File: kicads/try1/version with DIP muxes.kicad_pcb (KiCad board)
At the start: 2 copper layers, 166.5 x 100 mm, 48 parts, among them P1 CONN_01X08, P10 CONN_01X08, P11 CONN_01X08, P12 CONN_01X08, P13 CONN_01X08, P14 CONN_01X08, P15 CONN_01X08, P16 CONN_01X08, P17 CONN_01X08, P18 CONN_01X08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

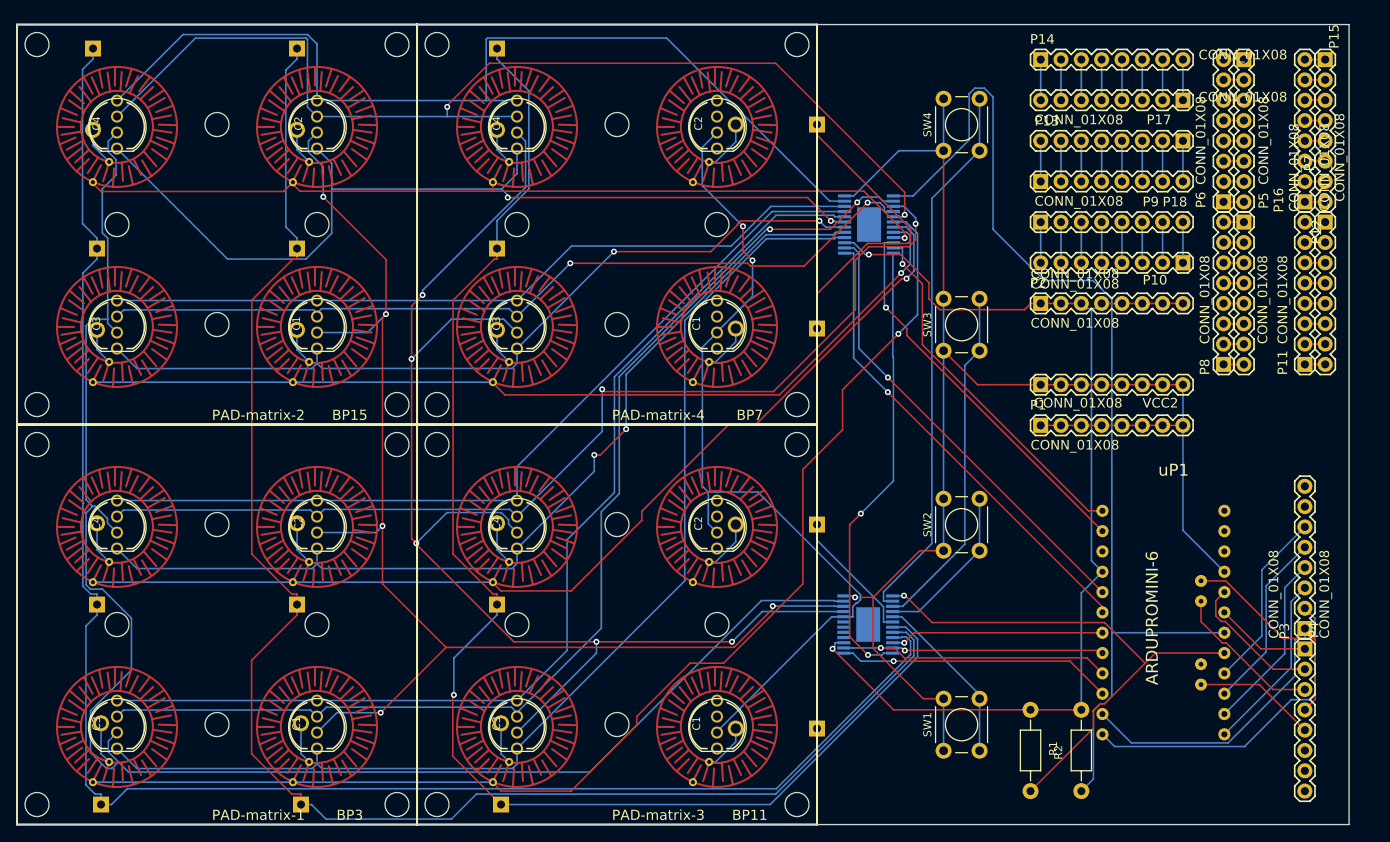
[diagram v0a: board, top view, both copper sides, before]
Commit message: successfully adapted the software for screen+button pad matrix using 16x muxes and arduino
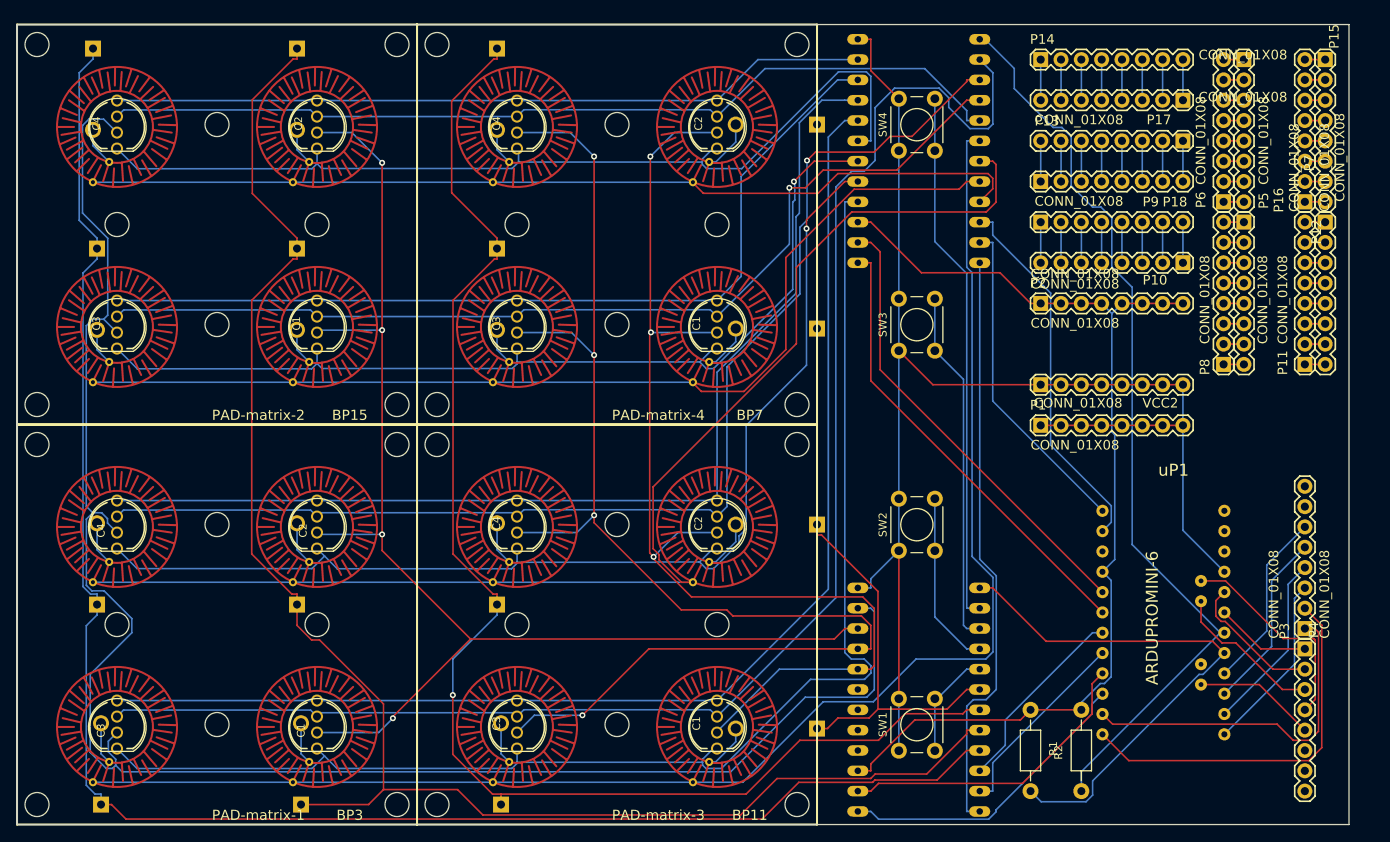
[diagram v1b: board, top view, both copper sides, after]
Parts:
- U2, U3: footprint SparkFun-DigitalIC:TSSOP-24 -> SparkFun-DigitalIC:DIL24-6
- moved U3 11.3 mm to (172.7, 135.9)
- moved U2 11.1 mm to (172.7, 67.3)
- moved SW1 5.59 mm to (170.2, 142.3)
- moved SW2 5.59 mm to (170.2, 117.3)
- moved SW3 5.59 mm to (170.2, 92.3)
- moved SW4 5.59 mm to (170.2, 67.3)
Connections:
- PAD-matrix-3 pad BLU1: Net-(PAD-matrix-3-PadBLU1) -> /MUXAB7
- PAD-matrix-3 pad BLU2: Net-(PAD-matrix-3-PadBLU2) -> /MUXAB6
- PAD-matrix-3 pad GRN1: Net-(PAD-matrix-3-PadGRN1) -> /MUXAG11
- PAD-matrix-3 pad GRN2: Net-(PAD-matrix-3-PadGRN2) -> /MUXAG10
- PAD-matrix-3 pad RED1: Net-(PAD-matrix-3-PadRED1) -> /MUXAR15
- PAD-matrix-3 pad RED2: Net-(PAD-matrix-3-PadRED2) -> /MUXAR14
- PAD-matrix-3 pad SIG1: Net-(PAD-matrix-3-PadSIG1) -> /MUXAS3
- PAD-matrix-3 pad SIG3: Net-(PAD-matrix-3-PadSIG3) -> /MUXAS2
- PAD-matrix-4 pad BLU1: Net-(PAD-matrix-4-PadBLU1) -> /MUXAB5
- PAD-matrix-4 pad BLU2: Net-(PAD-matrix-4-PadBLU2) -> /MUXAB4
- PAD-matrix-4 pad GRN1: Net-(PAD-matrix-4-PadGRN1) -> /MUXAG9
- PAD-matrix-4 pad GRN2: Net-(PAD-matrix-4-PadGRN2) -> /MUXAG8
- PAD-matrix-4 pad RED1: Net-(PAD-matrix-4-PadRED1) -> /MUXAR13
- PAD-matrix-4 pad RED2: Net-(PAD-matrix-4-PadRED2) -> /MUXAR12
- PAD-matrix-4 pad SIG1: Net-(PAD-matrix-4-PadSIG1) -> /MUXAS1
- PAD-matrix-4 pad SIG3: Net-(PAD-matrix-4-PadSIG3) -> /MUXAS0
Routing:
- net /MUXAB7: track 143.0 -> 189.5 mm, vias 2 -> 0
- net /MUXAS3: track 154.0 -> 186.1 mm, vias 1 -> 0
- net /MUXAS2: track 127.8 -> 159.9 mm, vias 1 -> 0
- net /MUXBG11: track 107.3 -> 138.1 mm, vias 2 -> 3
- net /MUXAR15: track 142.1 -> 171.0 mm
- net /MUXAG8: track 121.9 -> 94.7 mm
- net /MUXAG10: track 108.4 -> 135.0 mm
- net /MUXAB6: track 128.7 -> 151.8 mm, vias 2 -> 1
- net /MUXAG11: track 132.7 -> 155.7 mm
- net /MUXAR14: track 118.1 -> 140.4 mm, vias 2 -> 1
- net /MUXAB4: track 134.8 -> 115.1 mm, vias 2 -> 0
- net /MUXAB5: track 105.6 -> 124.6 mm, vias 2 -> 1
- net /A1: track 134.3 -> 115.8 mm
- net GND: track 56.7 -> 73.5 mm, vias 2 -> 0
- net /MUXAR13: track 103.5 -> 120.0 mm, vias 2 -> 1
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
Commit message: adapt portb connection to fit an LCD breakout
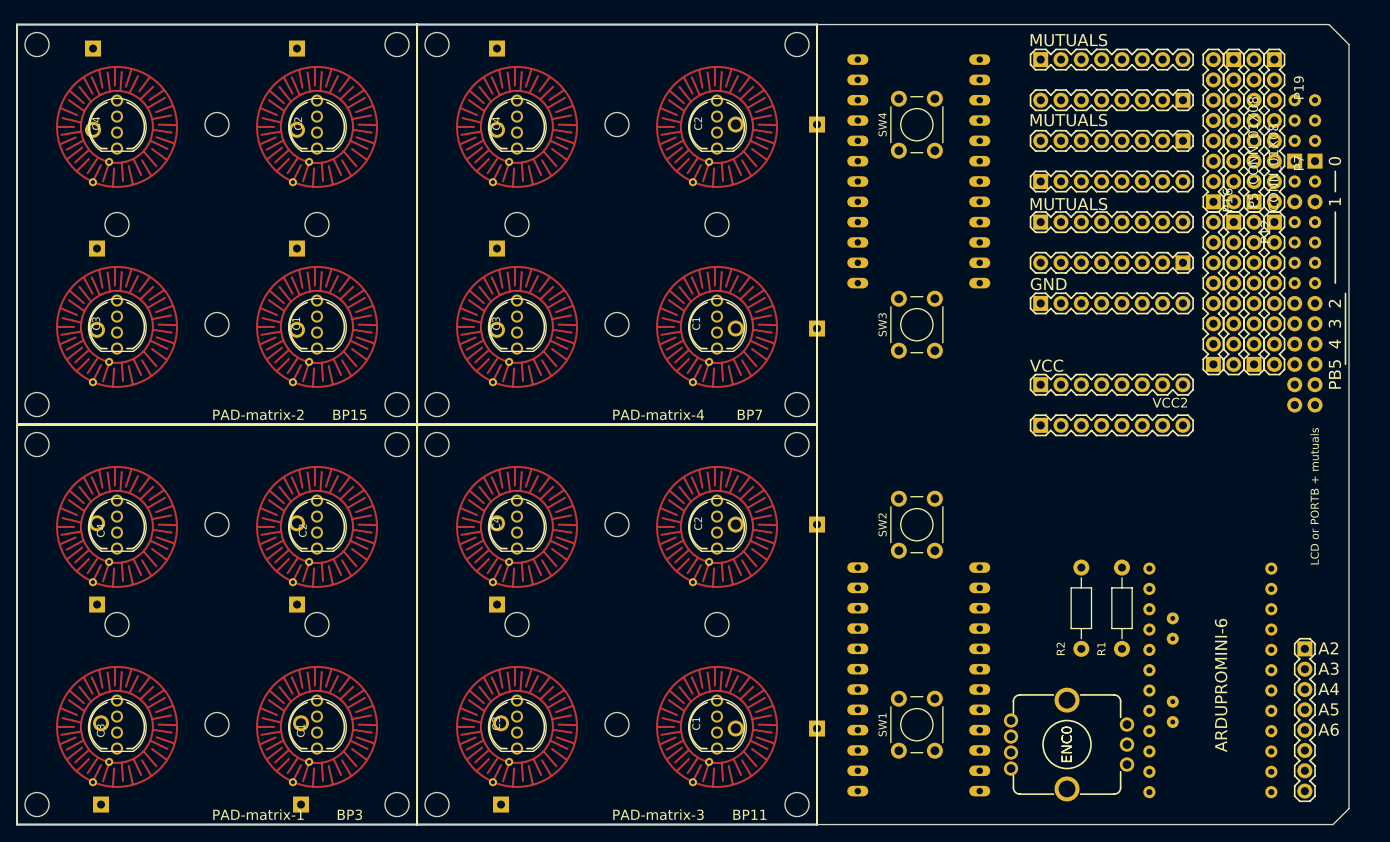
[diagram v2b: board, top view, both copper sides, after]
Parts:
- added ENC0: ENC0, SparkFun-Electromechanical:ENCODER_LED_2, F.Cu at (191.2, 141.5)
- added P19: CONN_01X16, lcd32-breakout-connector:1X08, F.Cu at (219.7, 61.0)
- P3: value CONN_01X08 -> CONN_01X16
- moved P3 66.1 mm to (222.2, 61.0), turned to 270 degrees
- moved uP1 54.6 mm to (219.3, 153.8), turned to 180 degrees
- moved R2 18.9 mm to (193.0, 119.4)
- moved R1 18.5 mm to (198.1, 129.5)
- moved P12 6.35 mm to (217.2, 76.2)
- moved P15 6.35 mm to (217.2, 55.9)
- moved P11 6.35 mm to (214.6, 94.0)
- moved P16 6.35 mm to (214.6, 73.7)
- moved U2 2.54 mm to (172.7, 69.8)
- moved U3 2.54 mm to (172.7, 133.3)
- moved P5 1.27 mm to (212.1, 55.9)
- moved P7 1.27 mm to (212.1, 76.2)
- moved P6 1.27 mm to (209.6, 73.7)
- moved P8 1.27 mm to (209.6, 94.0)
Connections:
- P13 pad 1: Net-(P13-Pad1) -> /MUX12
- P13 pad 2: Net-(P13-Pad2) -> /MUX13
- P13 pad 3: Net-(P13-Pad3) -> /MUX14
- P13 pad 4: Net-(P13-Pad4) -> /MUX15
- P14 pad 5: Net-(P13-Pad4) -> /MUX15
- P14 pad 6: Net-(P13-Pad3) -> /MUX14
- P14 pad 7: Net-(P13-Pad2) -> /MUX13
- P14 pad 8: Net-(P13-Pad1) -> /MUX12
- P2 pad 1: GNDREF -> GND
- P2 pad 2: GNDREF -> GND
- P2 pad 3: GNDREF -> GND
- P2 pad 4: GNDREF -> GND
- P2 pad 5: GNDREF -> GND
- P2 pad 6: GNDREF -> GND
- P2 pad 7: GNDREF -> GND
- P2 pad 8: GNDREF -> GND
- R1 pad 2: GNDREF -> GND
- R2 pad 1: GNDREF -> GND
- U2 pad 15: GNDREF -> GND
- U3 pad 15: GNDREF -> GND
- uP1 pad 10: GNDREF -> GND
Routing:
- net /MUXBG8: track 220.2 -> 0.00 mm
- net /MUXBS0: track 214.0 -> 0.00 mm
- net /MUXBS1: track 199.6 -> 0.00 mm
- net /MUXAB7: track 189.5 -> 0.00 mm
- net /MUXAS3: track 186.1 -> 0.00 mm
- net /VCC: track 180.3 -> 0.00 mm
- net /MUXBS2: track 174.1 -> 0.00 mm, vias 1 -> 0
- net /MUXAR15: track 171.0 -> 0.00 mm
- net /MUXBG10: track 169.4 -> 0.00 mm, vias 4 -> 0
- net /MUXBG9: track 163.4 -> 0.00 mm, vias 4 -> 0
- net /MUXAS2: track 159.9 -> 0.00 mm
- net /MUXAG11: track 155.7 -> 0.00 mm
- net /MUXAB6: track 151.8 -> 0.00 mm, vias 1 -> 0
- net /MUXAR14: track 140.4 -> 0.00 mm, vias 1 -> 0
- net /MUXBG11: track 138.1 -> 0.00 mm, vias 3 -> 0
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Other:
- outline, holes or cut-outs redrawn
- board text added: "0"
- board text added: "1"
- board text added: "2"
- board text added: "3"
- board text added: "4"
- board text added: "A2"
- board text added: "A3"
- board text added: "A4"
- board text added: "A5"
- board text added: "A6"
- board text added: "GND"
- board text added: "MUTUALS"
- board text added: "PB5"
- board text added: "VCC"

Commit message: routed last schematic change in the dip version
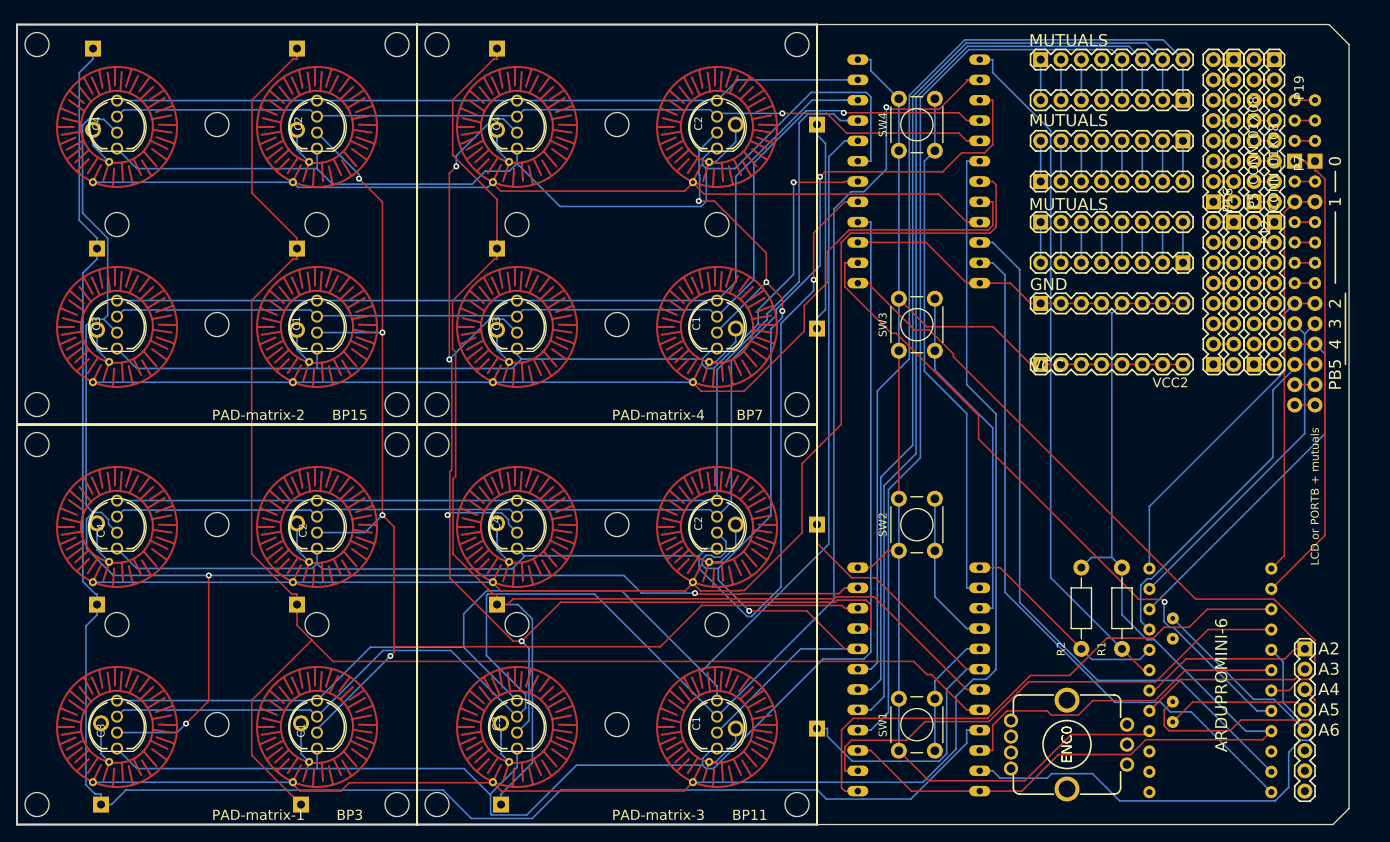
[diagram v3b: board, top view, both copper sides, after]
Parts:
- removed P1: CONN_01X08, SparkFun-Connectors:1X08
- moved CONN_01X08 2.54 mm to (188.0, 94.0)
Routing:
- net /MUXBS0: track 0.00 -> 218.0 mm
- net /MUXAB7: track 0.00 -> 209.6 mm, vias 0 -> 1
- net /MUXBS1: track 0.00 -> 198.3 mm
- net /MUXBG8: track 0.00 -> 196.7 mm, vias 0 -> 3
- net /MUXAS3: track 0.00 -> 191.2 mm
- net /MUXBS2: track 0.00 -> 177.5 mm
- net /MUXAR15: track 0.00 -> 176.0 mm
- net /MUXAG11: track 0.00 -> 174.6 mm
- net /VCC: track 0.00 -> 169.8 mm
- net GND: track 0.00 -> 168.9 mm
- net /MUXBG9: track 0.00 -> 160.5 mm, vias 0 -> 4
- net /MUXBG10: track 0.00 -> 160.5 mm, vias 0 -> 4
- net /MUXAS2: track 0.00 -> 159.0 mm
- net /MUXAB6: track 0.00 -> 155.3 mm, vias 0 -> 1
- net /MUXAR14: track 0.00 -> 149.8 mm, vias 0 -> 1
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
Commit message: tried to put ledmatrix libraries inside the libraries but couldn't because problems between static and instance modes that i don't understand
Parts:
- added hole1: MountingHole_3mm, Mounting_Holes:MountingHole_3mm, F.Cu at (224.0, 54.0)
- added hole2: hole2, Mounting_Holes:MountingHole_3mm, F.Cu at (224.0, 149.0)
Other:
- outline, holes or cut-outs redrawn
- board text added: "download this design SYNTH.AUTOTEL.CO"
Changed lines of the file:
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@@
     (links 251)
     (no_connects 0)
-    (area 59.949999 51.449999 226.550001 151.550001)
+    (area 59.233299 47.733299 231.417486 154.2502)
     (thickness 1.6)
-    (drawings 25)
+    (drawings 27)
     (tracks 926)
     (zones 0)
-    (modules 49)
+    (modules 51)
     (nets 142)
   )
@@
     (visible_elements 7FFFEFFF)
     (pcbplotparams
-      (layerselection 0x010fc_80000001)
-      (usegerberextensions false)
+      (layerselection 0x010f0_80000001)
+      (usegerberextensions true)
       (excludeedgelayer true)
       (linewidth 0.100000)
@@
       (drillshape 0)
       (scaleselection 1)
-      (outputdirectory "plot jobs 2/"))
+      (outputdirectory "plot jobs dip version/"))
   )
   (net 0 "")
@@
     (pad SW thru_hole circle (at -3 -7 90) (size 1.778 1.778) (drill 1.1) (layers *.Cu *.Mask))
   )
+  (module Mounting_Holes:MountingHole_3mm (layer F.Cu)
+    (at 224 149)
+    (descr "Mounting Hole 3mm, no annular")
+    (tags "mounting hole 3mm no annular")
+    (fp_text reference hole2 (at 0 -4) (layer F.SilkS)
+      (effects (font (size 1 1) (thickness 0.15)))
+    )
+    (fp_text value hole2 (at 0 4) (layer F.Fab)
+      (effects (font (size 1 1) (thickness 0.15)))
+    )
+    (fp_circle (center 0 0) (end 3 0) (layer Cmts.User) (width 0.15))
+    (fp_circle (center 0 0) (end 3.25 0) (layer F.CrtYd) (width 0.05))
+    (pad 1 np_thru_hole circle (at 0 0) (size 3 3) (drill 3) (layers *.Cu *.Mask))
+  )
+  (module Mounting_Holes:MountingHole_3mm (layer F.Cu)
+    (at 224 54)
+    (descr "Mounting Hole 3mm, no annular")
+    (tags "mounting hole 3mm no annular")
+    (fp_text reference hole1 (at 0 -4) (layer F.SilkS) hide
+      (effects (font (size 1 1) (thickness 0.15)))
+    )
+    (fp_text value MountingHole_3mm (at 0 4) (layer F.Fab) hide
+      (effects (font (size 1 1) (thickness 0.15)))
+    )
+    (fp_circle (center 0 0) (end 3 0) (layer Cmts.User) (width 0.15))
+    (fp_circle (center 0 0) (end 3.25 0) (layer F.CrtYd) (width 0.05))
+    (pad 1 np_thru_hole circle (at 0 0) (size 3 3) (drill 3) (layers *.Cu *.Mask))
+  )
+  (dimension 166.5 (width 0.3) (layer B.SilkS)
+    (gr_text "166,500 mm" (at 143.25 44.65) (layer B.SilkS)
+      (effects (font (size 1.5 1.5) (thickness 0.3)))
+    )
+    (feature1 (pts (xy 226.5 48.5) (xy 226.5 43.3)))
+    (feature2 (pts (xy 60 48.5) (xy 60 43.3)))
+    (crossbar (pts (xy 60 46) (xy 226.5 46)))
+    (arrow1a (pts (xy 226.5 46) (xy 225.373496 46.586421)))
+    (arrow1b (pts (xy 226.5 46) (xy 225.373496 45.413579)))
+    (arrow2a (pts (xy 60 46) (xy 61.126504 46.586421)))
+    (arrow2b (pts (xy 60 46) (xy 61.126504 45.413579)))
+  )
+  (gr_text "download this design\nSYNTH.AUTOTEL.CO" (at 211 148.5 270) (layer B.SilkS)
+    (effects (font (size 2 2) (thickness 0.3)) (justify left mirror))
+  )
   (gr_line (start 224.79 83.82) (end 224.79 74.93) (angle 90) (layer F.SilkS) (width 0.2))
   (gr_line (start 224.79 72.39) (end 224.79 69.85) (angle 90) (layer F.SilkS) (width 0.2))
@@
   )
   (gr_line (start 226.5 149.5) (end 224.5 151.5) (layer Edge.Cuts) (width 0.1))
-  (gr_line (start 224 51.5) (end 226.5 54) (layer Edge.Cuts) (width 0.1))
+  (gr_line (start 224.5 51.5) (end 226.5 53.5) (layer Edge.Cuts) (width 0.1))
   (gr_line (start 60 151.5) (end 60 51.5) (layer Edge.Cuts) (width 0.1))
   (gr_line (start 224.5 151.5) (end 60 151.5) (layer Edge.Cuts) (width 0.1))
-  (gr_line (start 226.5 54) (end 226.5 149.5) (layer Edge.Cuts) (width 0.1))
-  (gr_line (start 60 51.5) (end 224 51.5) (angle 90) (layer Edge.Cuts) (width 0.1))
+  (gr_line (start 226.5 53.5) (end 226.5 149.5) (layer Edge.Cuts) (width 0.1))
+  (gr_line (start 60 51.5) (end 224.5 51.5) (angle 90) (layer Edge.Cuts) (width 0.1))
   (segment (start 70.5025 142.656) (end 70.5025 138.84) (width 0.2032) (layer B.Cu) (net 1))
   (segment (start 71.519 143.672) (end 70.5025 142.656) (width 0.2032) (layer B.Cu) (net 1))
